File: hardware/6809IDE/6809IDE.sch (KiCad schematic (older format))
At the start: 20 parts, among them J1 SS50-LIKE, J2 Mem Addr, J3 Drive 0, J6 Drive 0, U1 74HC245, U2 74HC245

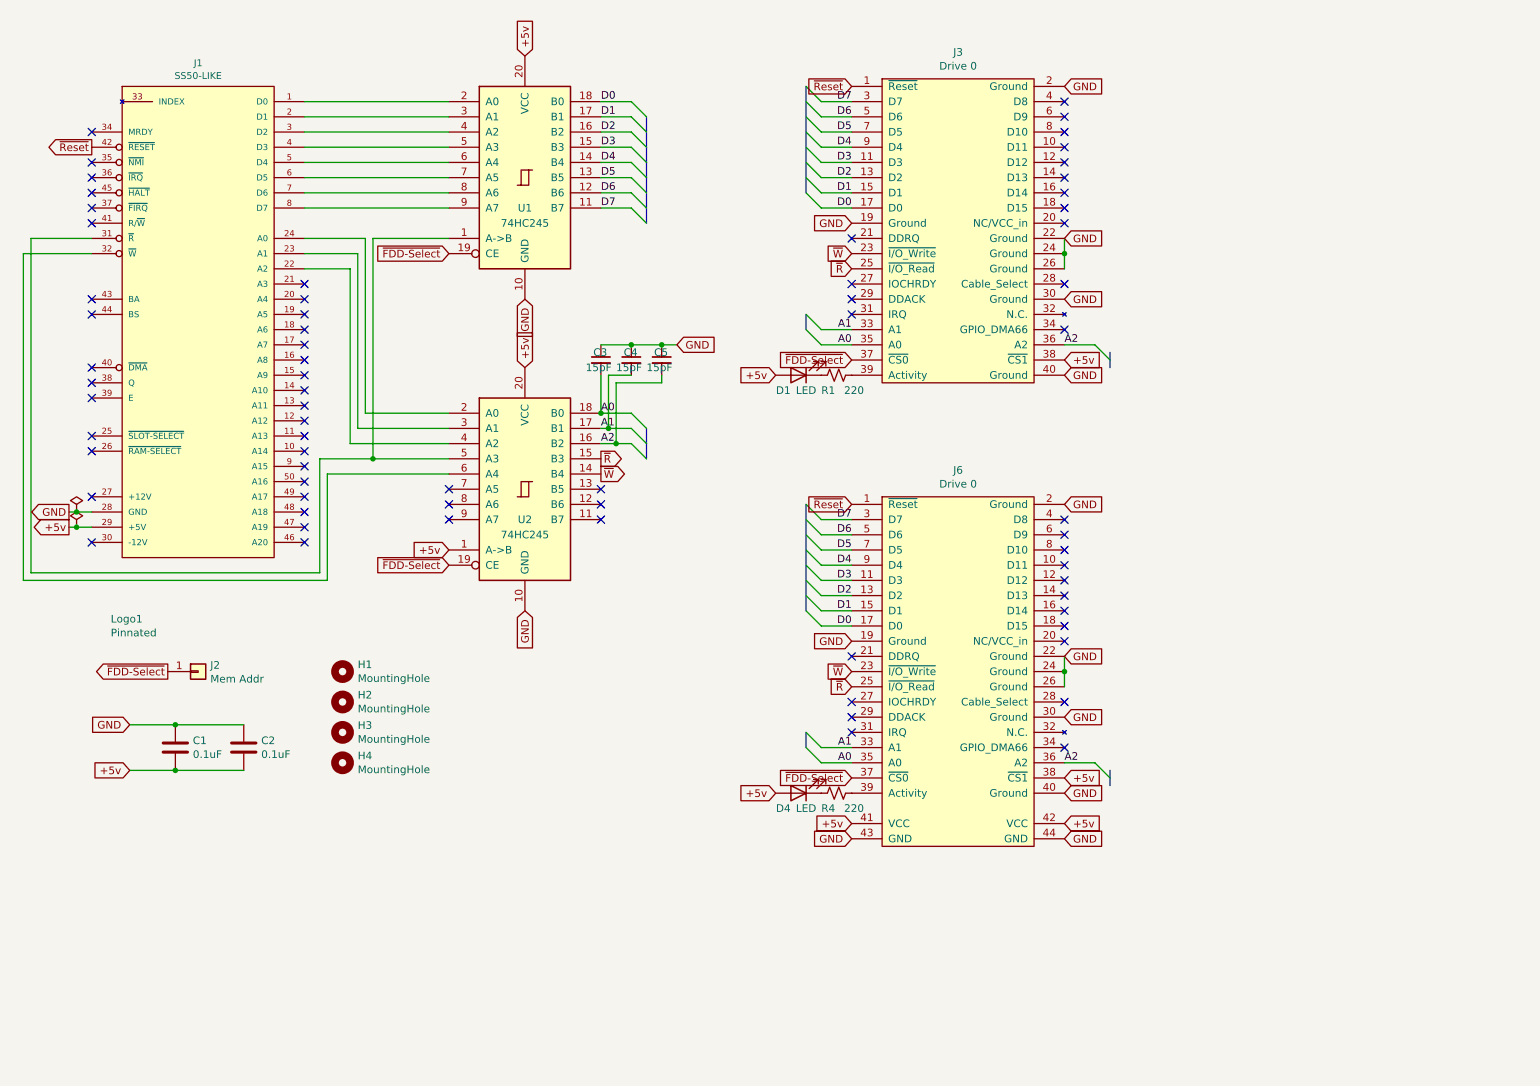
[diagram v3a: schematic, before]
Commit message: start of ROM and RAM board
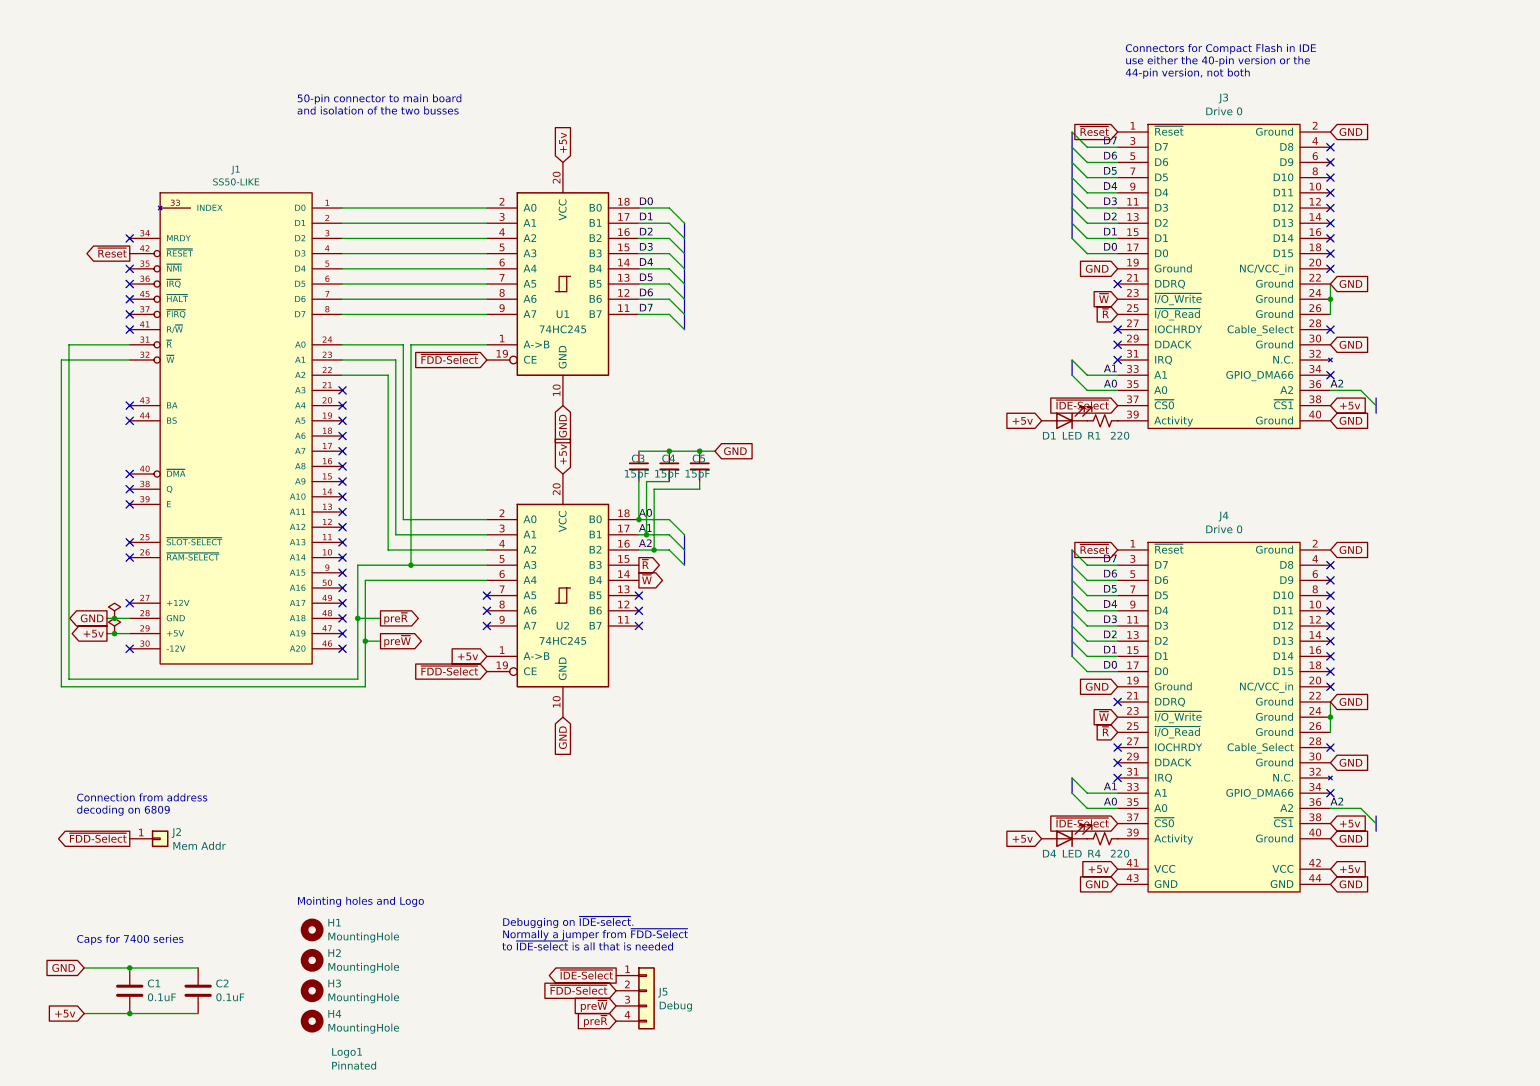
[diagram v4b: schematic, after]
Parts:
- added J5: Debug, Connector_PinHeader_2.54mm:PinHeader_1x04_P2.54mm_Vertical, symbol Connector_Generic:Conn_01x04
- renumbered J6 to J4
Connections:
- net ~FDD-Select: now also J5.2 (Pin_2); no longer J3.37 (~CS0), J4.37 (~CS0)
- net pre~R: now reaches J1.31 (~R), U1.1 (A->B), U2.5 (A3)
- net pre~R: now also J5.4 (Pin_4)
- net pre~W: now reaches J1.32 (~W), U2.6 (A4)
- net pre~W: now also J5.3 (Pin_3)
- new net ~IDE-Select: J3.37 (~CS0), J4.37 (~CS0), J5.1 (Pin_1)
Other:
- note added: "50-pin connector to main board\nand isolation of the two busses"
- note added: "Caps for 7400 series"
- note added: "Connection from address\ndecoding on 6809"
- note added: "Connectors for Compact Flash in IDE\nuse either the 40-pin version or the\n44-pin version, not both"
- note added: "Debugging on ~IDE-select~. \nNormally a jumper from ~FDD-Select~ \nto ~IDE-select~ is all that is needed"
- note added: "Mointing holes and Logo"
- moved on the sheet: C1, C2, C3, C4, C5, D1, D4, H1, H2, H3, H4, J1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
